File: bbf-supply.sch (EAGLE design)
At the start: 18 parts, among them IC1 780X, IC2 LT1054, IC3 790X

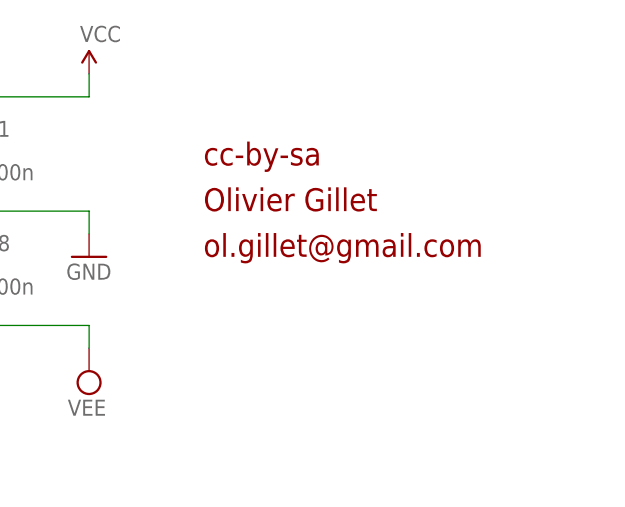
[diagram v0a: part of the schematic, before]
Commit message: update names on boards and schematics
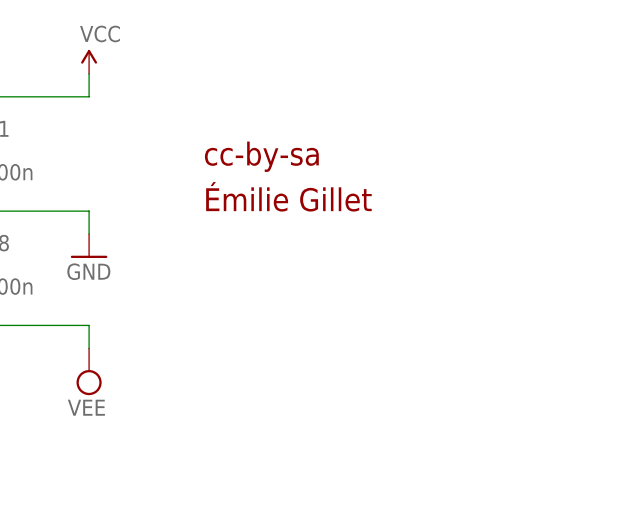
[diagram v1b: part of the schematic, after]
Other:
- note added: "Émilie Gillet"
- note removed: "Olivier Gillet"
- note removed: "ol.gillet@gmail.com"
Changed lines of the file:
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@@
 <plain>
 <text x="106.68" y="142.24" size="2.54" layer="94">cc-by-sa</text>
-<text x="106.68" y="137.16" size="2.54" layer="94">Olivier Gillet</text>
-<text x="106.68" y="132.08" size="2.54" layer="94">ol.gillet@gmail.com</text>
+<text x="106.68" y="137.16" size="2.54" layer="94">Émilie Gillet</text>
 <text x="33.02" y="154.94" size="1.778" layer="97">+/- 5V supply</text>
 </plain>
